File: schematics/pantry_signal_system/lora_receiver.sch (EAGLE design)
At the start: 3 parts, among them J1 JST-XH254-2P, U1 ESP32, U12 E220-900T22D

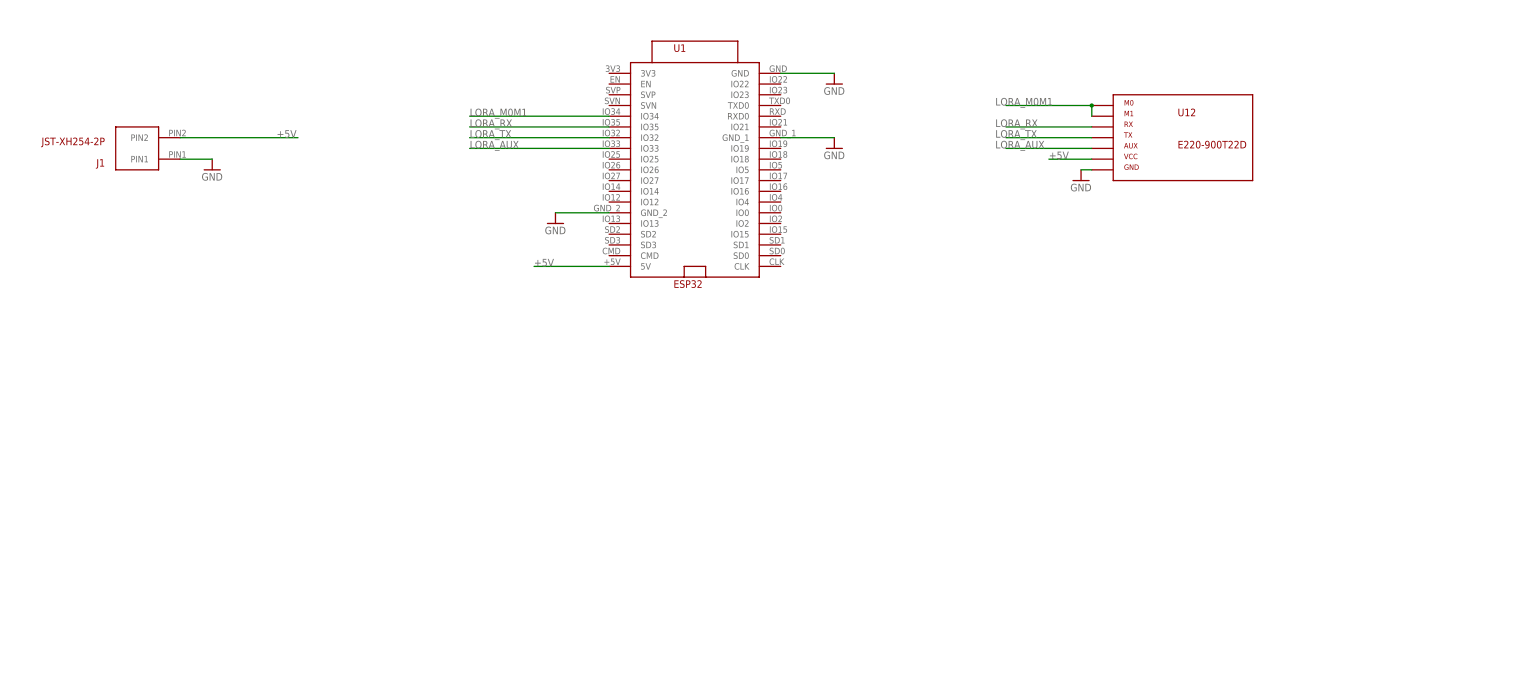
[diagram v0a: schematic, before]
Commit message: Fix problem with signal level 3V3 <-> 5V for lora
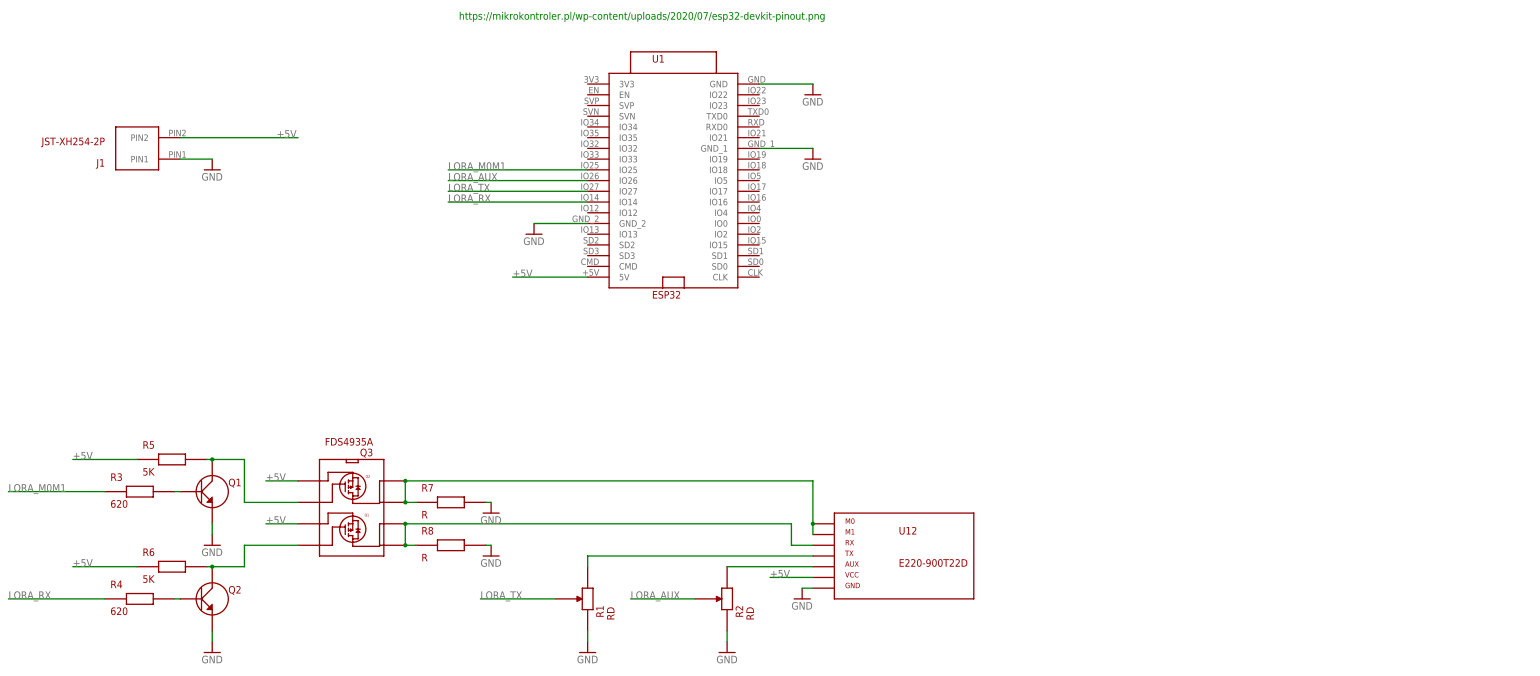
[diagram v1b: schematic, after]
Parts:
- added Q1, Q2: (no value), my_devices:TRANSISTOR_NPN
- added Q3: FDS4935A, my_devices:MOSFET_P_X2
- added R1, R2: RD, my_devices:RD
- added R3, R4: 620, my_devices:R
- added R5, R6: 5K, my_devices:R
- added R7, R8: R, my_devices:R
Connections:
- new net N$1: R2.P2, U12.AUX
- new net N$2: R1.P2, U12.TX
- new net N$3: Q1.B, R3.P$2
- new net N$4: Q2.B, R4.P$2
- new net N$5: Q1.C, Q3.G2, R5.P$2
- new net N$6: Q2.C, Q3.G1, R6.P$2
- new net N$8: Q3.D11, Q3.D12, R8.P$1, U12.RX
- new net N$9: Q3.D21, Q3.D22, R7.P$1, U12.M0, U12.M1
- net +5V: now also Q3.S1, Q3.S2, R5.P$1, R6.P$1
- net GND: now also Q1.E, Q2.E, R1.P1, R2.P1, R7.P$2, R8.P$2
- net LORA_AUX: now also R2.P3, U1.IO26; no longer U1.IO33, U12.AUX
- net LORA_M0M1: now also R3.P$1, U1.IO25; no longer U1.IO34, U12.M0, U12.M1
- net LORA_RX: now also R4.P$1, U1.IO14; no longer U1.IO35, U12.RX
- net LORA_TX: now also R1.P3, U1.IO27; no longer U1.IO32, U12.TX
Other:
- note added: "https://mikrokontroler.pl/wp-content/uploads/2020/07/esp32-devkit-pinout.png"
- moved on the sheet: U1, U12

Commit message: Preparing primary schema for creating board - all packages setup
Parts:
- R1, R2: value RD -> 10K
- R7, R8: value R -> 5K
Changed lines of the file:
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@@
 <part name="J1" library="my_devices" deviceset="JST-XH254-2P" device=""/>
 <part name="GND4" library="supply1" library_urn="urn:adsk.eagle:library:371" deviceset="GND" device=""/>
-<part name="R1" library="my_devices" deviceset="RD" device=""/>
-<part name="R2" library="my_devices" deviceset="RD" device=""/>
+<part name="R1" library="my_devices" deviceset="RD" device="" value="10K"/>
+<part name="R2" library="my_devices" deviceset="RD" device="" value="10K"/>
 <part name="GND5" library="supply1" library_urn="urn:adsk.eagle:library:371" deviceset="GND" device=""/>
 <part name="GND6" library="supply1" library_urn="urn:adsk.eagle:library:371" deviceset="GND" device=""/>
@@
 <part name="R6" library="my_devices" deviceset="R" device="" value="5K"/>
 <part name="Q3" library="my_devices" deviceset="MOSFET_P_X2" device="" value="FDS4935A"/>
-<part name="R7" library="my_devices" deviceset="R" device=""/>
-<part name="R8" library="my_devices" deviceset="R" device=""/>
+<part name="R7" library="my_devices" deviceset="R" device="" value="5K"/>
+<part name="R8" library="my_devices" deviceset="R" device="" value="5K"/>
 <part name="GND9" library="supply1" library_urn="urn:adsk.eagle:library:371" deviceset="GND" device=""/>
 <part name="GND10" library="supply1" library_urn="urn:adsk.eagle:library:371" deviceset="GND" device=""/>

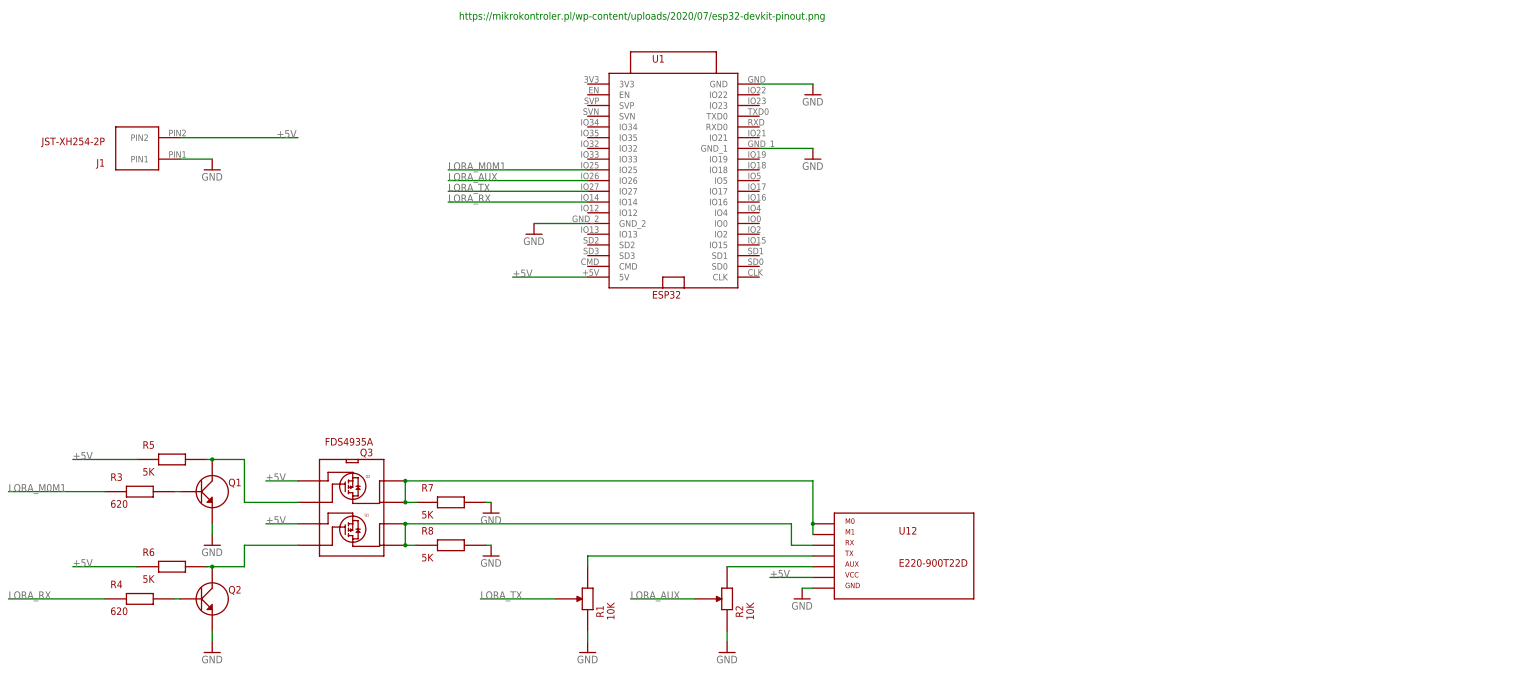
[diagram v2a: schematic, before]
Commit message: Changed LoRa Receiver schematics to use level converter modules
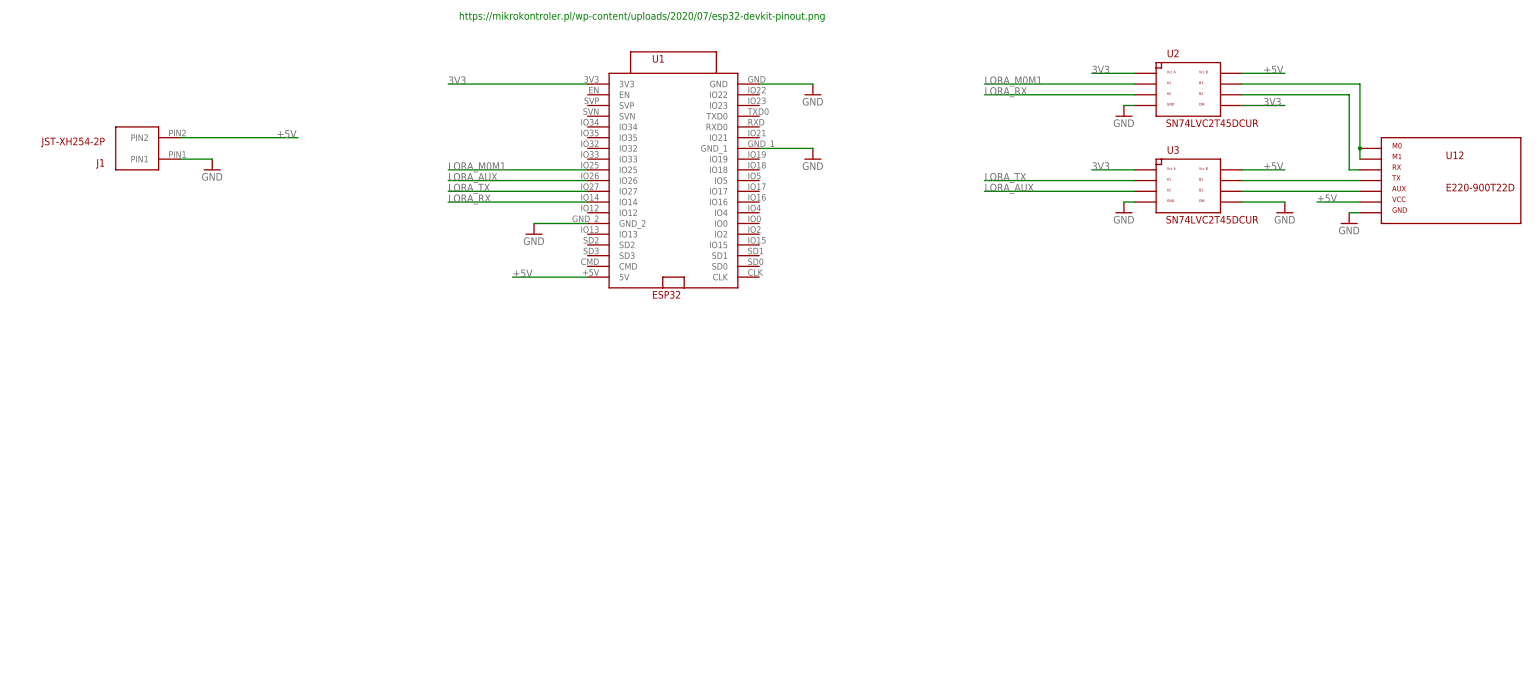
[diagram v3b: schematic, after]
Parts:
- removed Q1, Q2: (no value), my_devices:TRANSISTOR_NPN
- removed Q3: FDS4935A, my_devices:MOSFET_P_X2
- removed R1, R2: 10K, my_devices:RD
- removed R3, R4: 620, my_devices:R
- removed R5, R6, R7, R8: 5K, my_devices:R
- added U2, U3: SN74LVC2T45DCUR, my_devices:LEVEL_CONVERTER_2L
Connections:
- removed net N$4: Q2.B, R4.P$2
- removed net N$5: Q1.C, Q3.G2, R5.P$2
- removed net N$6: Q2.C, Q3.G1, R6.P$2
- removed net N$8: Q3.D11, Q3.D12, R8.P$1, U12.RX
- new net 3V3: U1.3V3, U2.DIR, U2.VCCA, U3.VCCA
- net +5V: now also U2.VCCB, U3.VCCB; no longer Q3.S1, Q3.S2, R5.P$1, R6.P$1
- net GND: now also U2.GND, U3.DIR, U3.GND; no longer Q1.E, Q2.E, R1.P1, R2.P1, R7.P$2, R8.P$2
- net LORA_AUX: now also U3.A2; no longer R2.P3
- net LORA_M0M1: now also U2.A1; no longer R3.P$1
- net LORA_RX: now also U2.A2; no longer R4.P$1
- net LORA_TX: now also U3.A1; no longer R1.P3
- net N$1: now also U12.TX, U3.B1; no longer R2.P2, U12.AUX
- net N$2: now also U12.RX, U2.B2; no longer R1.P2, U12.TX
- net N$3: now also U12.AUX, U3.B2; no longer Q1.B, R3.P$2
- net N$9: now also U2.B1; no longer Q3.D21, Q3.D22, R7.P$1
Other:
- moved on the sheet: U12

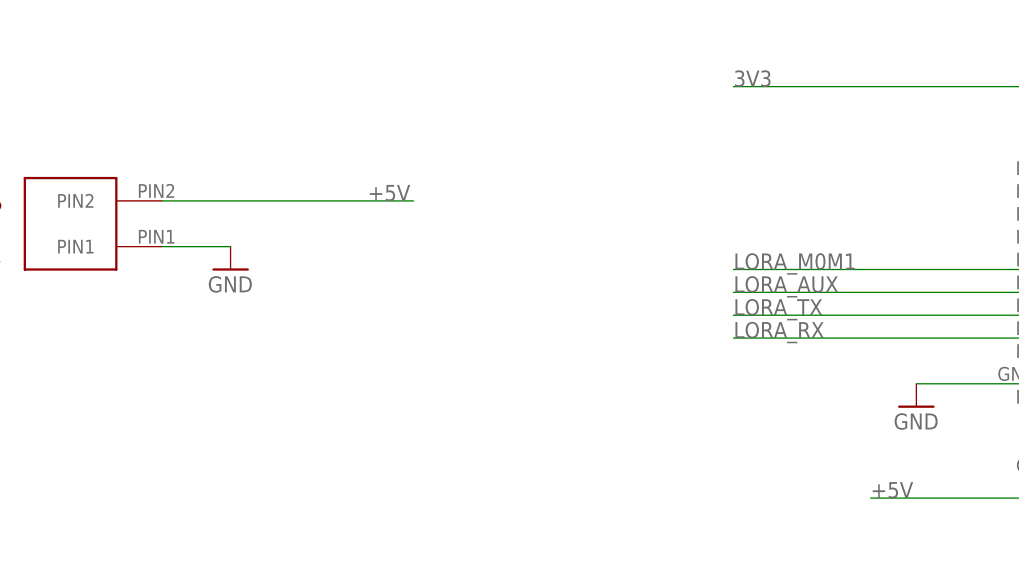
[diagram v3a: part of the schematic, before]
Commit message: Added board for LoRa receiver
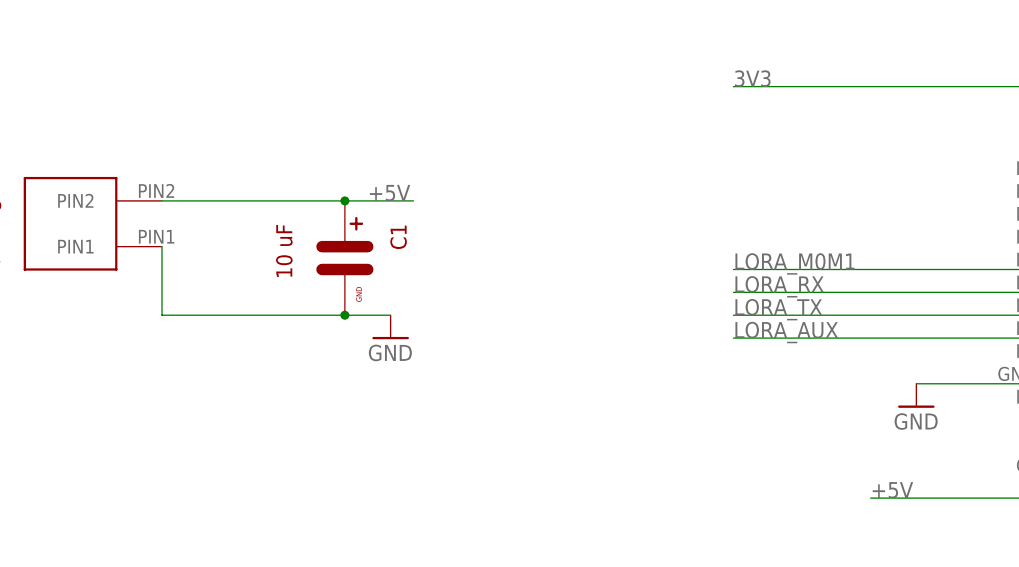
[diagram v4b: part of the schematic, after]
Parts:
- added C1: 10 uF, my_devices:CMINI-5X7
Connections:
- net +5V: now also C1.PIN_PLUS
- net GND: now also C1.PIN_GND
- net LORA_AUX: now also U1.IO14; no longer U1.IO26
- net LORA_RX: now also U1.IO26; no longer U1.IO14
